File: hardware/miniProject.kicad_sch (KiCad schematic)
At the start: 6 parts, among them J1 ENCODER, SW1 BACKBUTTON, U1 ESP32-WROOM-32E, U2 NRF24L01, U3 OLED SCREEN

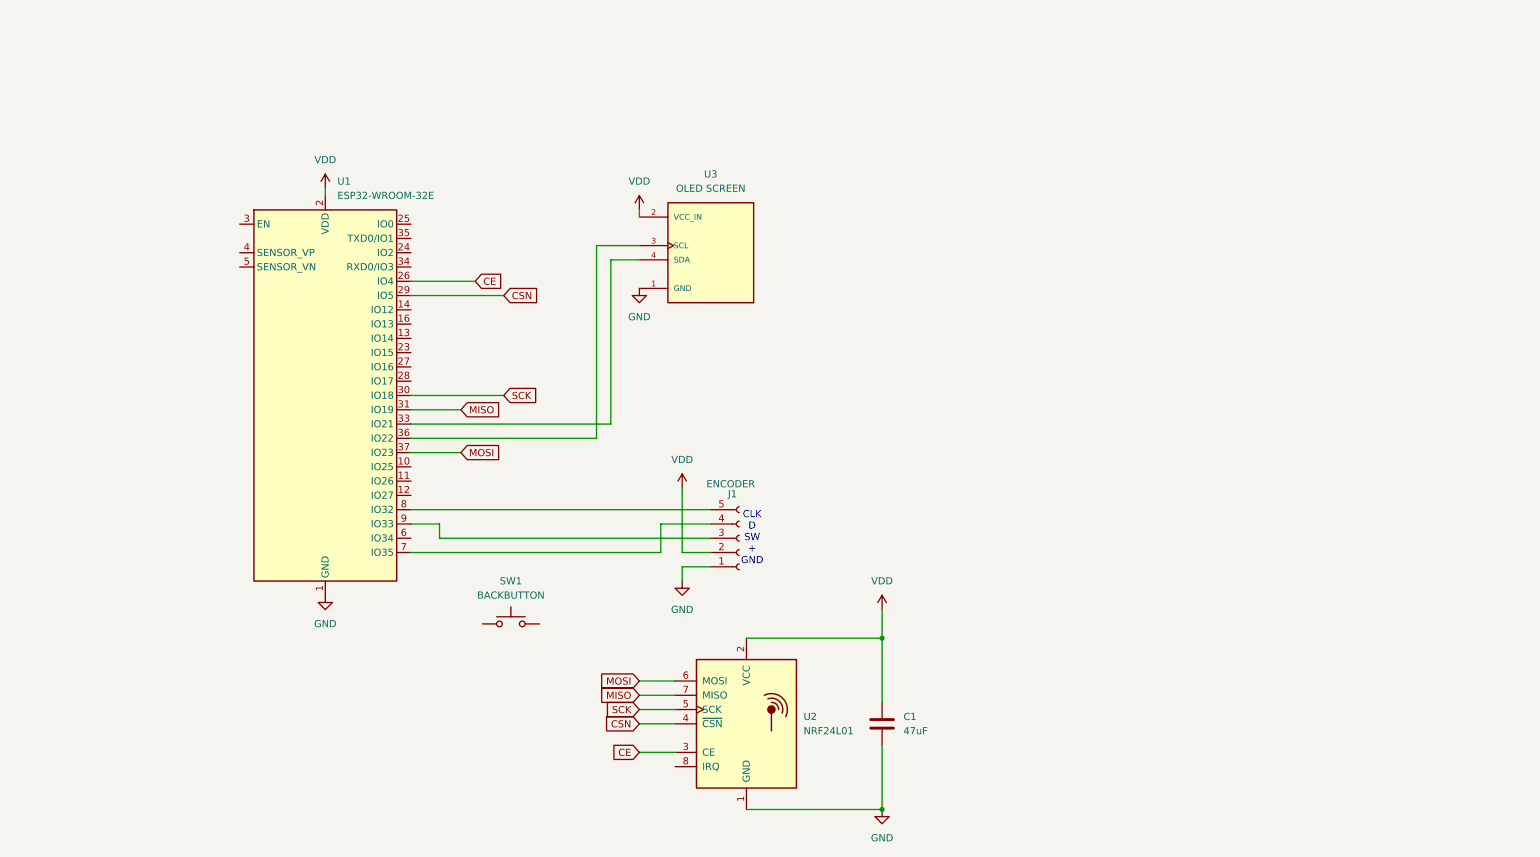
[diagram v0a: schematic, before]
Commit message: Added speaker circuitry
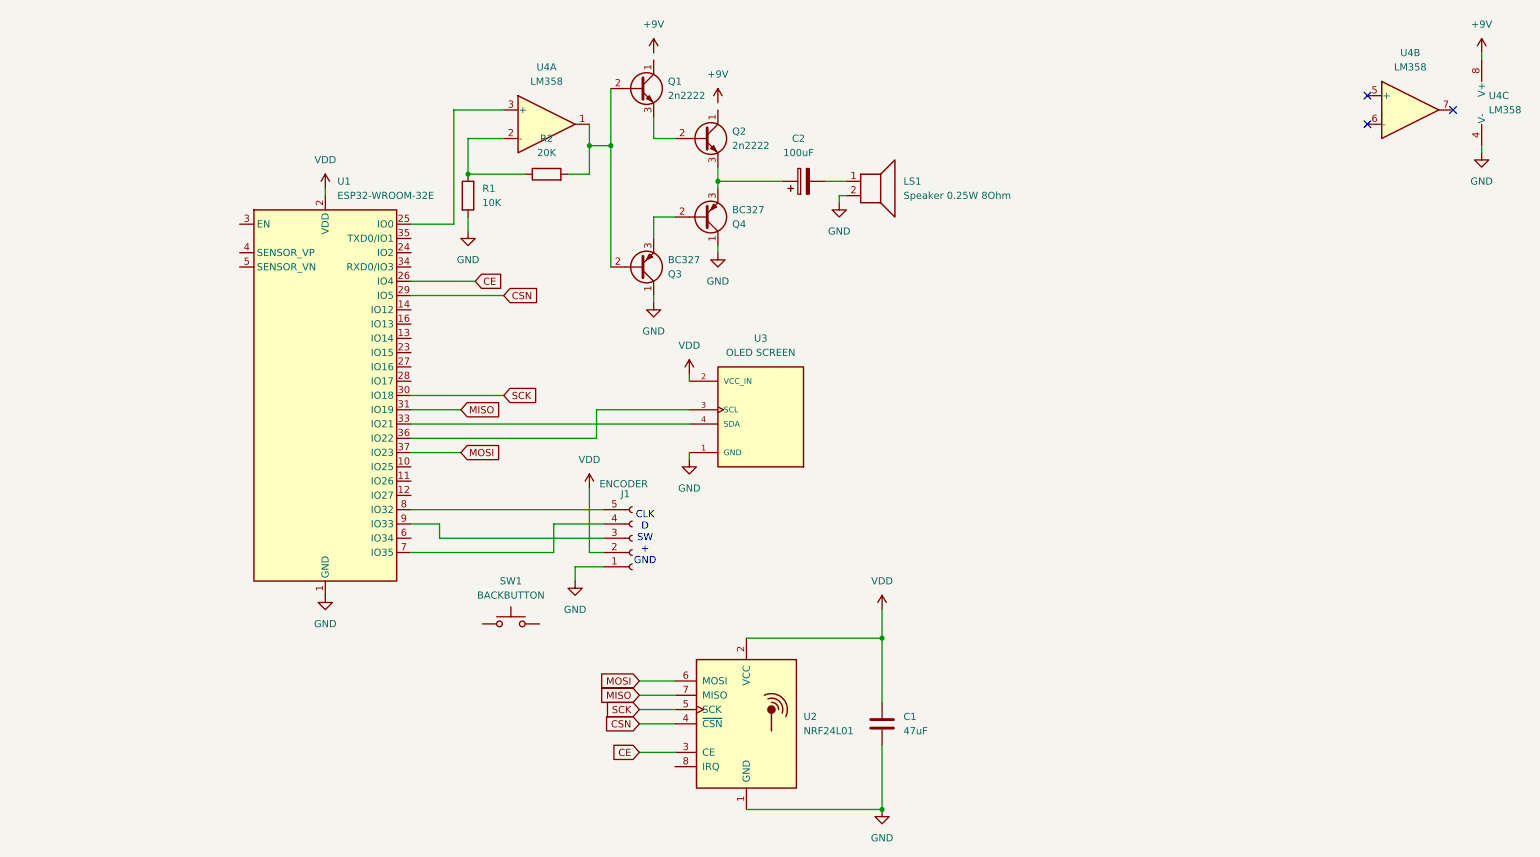
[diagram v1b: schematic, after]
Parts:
- added C2: 100uF, symbol Device:C_Polarized
- added LS1: Speaker 0.25W 8Ohm, symbol Device:Speaker
- added Q1, Q2: 2n2222, Package_TO_SOT_THT:TO-92_Inline, symbol Transistor_BJT:BC337
- added Q3, Q4: BC327, Package_TO_SOT_THT:TO-92_Inline, symbol Transistor_BJT:BC327
- added R1: 10K, symbol Device:R
- added R2: 20K, symbol Device:R
- added U4: LM358, symbol Amplifier_Operational:LM358
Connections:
- net GND: now also LS1.2, Q3.1 (C), Q4.1 (C), R1.2, U4.4 (V-)
- net at U1.25 (IO0): now also U4.3 (+)
- new net: C2.2, LS1.1
- new net: Q1.3 (E), Q2.2 (B)
- new net: C2.1, Q2.3 (E), Q4.3 (E)
- new net: R1.1, R2.1, U4.2 (-)
- new net: Q1.2 (B), Q3.2 (B), R2.2, U4.1
- new net: Q3.3 (E), Q4.2 (B)
- new net +9V: U4.8 (V+)
- no-connect marks 0 -> 3
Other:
- moved on the sheet: J1, U3

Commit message: fix: minor convenience fixes
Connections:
- net +9V: now also Q1.1 (C), Q2.1 (C)
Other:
- note added: "Second opamp in ic"
- moved on the sheet: C1, U2, U4B, U4C

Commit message: feat: add tiny pcb test
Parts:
- removed SW1: BACKBUTTON, symbol Switch:SW_Push
- C1, C2: footprint (none) -> Capacitor_THT:CP_Axial_L10.0mm_D4.5mm_P15.00mm_Horizontal
- J1: footprint (none) -> Rotary_Encoder:RotaryEncoder_Alps_EC12E-Switch_Vertical_H20mm
- LS1: footprint (none) -> Buzzer_Beeper:Speaker_CUI_CMR-1206S-67
- R1, R2: footprint (none) -> Resistor_THT:R_Axial_DIN0204_L3.6mm_D1.6mm_P1.90mm_Vertical
- U3: footprint DM-OLED096-636:MODULE_DM-OLED096-636 -> SH1106:MODULE_DM-OLED096-636
- U4: footprint (none) -> Package_DIP:DIP-8_W7.62mm
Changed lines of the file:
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@@
 			)
 		)
-		(property "Footprint" ""
+		(property "Footprint" "Rotary_Encoder:RotaryEncoder_Alps_EC12E-Switch_Vertical_H20mm"
 			(at 124.46 105.41 0)
 			(effects
@@
 			)
 		)
-		(property "Footprint" ""
+		(property "Footprint" "Buzzer_Beeper:Speaker_CUI_CMR-1206S-67"
 			(at 167.64 46.99 0)
 			(effects
@@
 			)
 		)
-		(property "Footprint" ""
+		(property "Footprint" "Package_DIP:DIP-8_W7.62mm"
 			(at 22.86 31.75 0)
 			(effects
@@
 			)
 		)
-		(property "Footprint" ""
+		(property "Footprint" "Resistor_THT:R_Axial_DIN0204_L3.6mm_D1.6mm_P1.90mm_Vertical"
 			(at 109.22 42.418 90)
 			(effects
@@
 			)
 		)
-		(property "Footprint" ""
+		(property "Footprint" "Resistor_THT:R_Axial_DIN0204_L3.6mm_D1.6mm_P1.90mm_Vertical"
 			(at 93.472 44.45 90)
 			(effects
@@
 				(path "/4236fcd5-e68f-4547-b2f6-dcd9c792f255"
 					(reference "#PWR08")
-					(unit 1)
-				)
-			)
-		)
-	)
-	(symbol
-		(lib_id "Switch:SW_Push")
-		(at 102.87 120.65 0)
-		(unit 1)
-		(exclude_from_sim no)
-		(in_bom yes)
-		(on_board yes)
-		(dnp no)
-		(fields_autoplaced yes)
-		(property "Reference" "SW1"
-			(at 102.87 113.03 0)
-			(effects
-				(font
-					(size 1.27 1.27)
-				)
-			)
-		)
-		(property "Value" "BACKBUTTON"
-			(at 102.87 115.57 0)
-			(effects
-				(font
-					(size 1.27 1.27)
-				)
-			)
-		)
-		(property "Footprint" ""
-			(at 102.87 115.57 0)
-			(effects
-				(font
-					(size 1.27 1.27)
-				)
-				(hide yes)
-			)
-		)
-		(property "Datasheet" "~"
-			(at 102.87 115.57 0)
-			(effects
-				(font
-					(size 1.27 1.27)
-				)
-				(hide yes)
-			)
-		)
-		(property "Description" "Push button switch, generic, two pins"
-			(at 102.87 120.65 0)
-			(effects
-				(font
-					(size 1.27 1.27)
-				)
-				(hide yes)
-			)
-		)
-		(pin "1"
-		)
-		(pin "2"
-		)
-		(instances
-			(project ""
-				(path "/4236fcd5-e68f-4547-b2f6-dcd9c792f255"
-					(reference "SW1")
 					(unit 1)
 				)
@@
 			)
 		)
-		(property "Footprint" "DM-OLED096-636:MODULE_DM-OLED096-636"
+		(property "Footprint" "SH1106:MODULE_DM-OLED096-636"
 			(at 147.32 85.09 0)
 			(effects
@@
 			)
 		)
-		(property "Footprint" ""
+		(property "Footprint" "Package_DIP:DIP-8_W7.62mm"
 			(at 38.1 30.48 0)
 			(effects
@@
 			)
 		)
-		(property "Footprint" ""
+		(property "Footprint" "Capacitor_THT:CP_Axial_L10.0mm_D4.5mm_P15.00mm_Horizontal"
 			(at 218.1352 91.44 0)
 			(effects
@@
 			)
 		)
-		(property "Footprint" ""
+		(property "Footprint" "Package_DIP:DIP-8_W7.62mm"
 			(at 109.22 31.75 0)
 			(effects
@@
 			)
 		)
-		(property "Footprint" ""
+		(property "Footprint" "Capacitor_THT:CP_Axial_L10.0mm_D4.5mm_P15.00mm_Horizontal"
 			(at 158.75 40.9448 0)
 			(effects
